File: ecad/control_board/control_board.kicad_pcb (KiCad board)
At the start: 2 copper layers, 40 x 51 mm, 49 parts, among them J1 USB_C_Receptacle_USB2.0_16P, J10 JST PH 3, J2 JST SH 3, J3 JST SH 3, J4 JST SH 3, J5 JST SH 3, J6 JST SH 3, J7 JST SH 3, J9 JST PH 3, Q6 RE1C002UN, U1 W25Q16JVUXIQ, U2 TLV75733PDBV, U3 RP2040, U4 TUSB320I, U5 TPS2552DRV, Y1 ABM8-272-T3

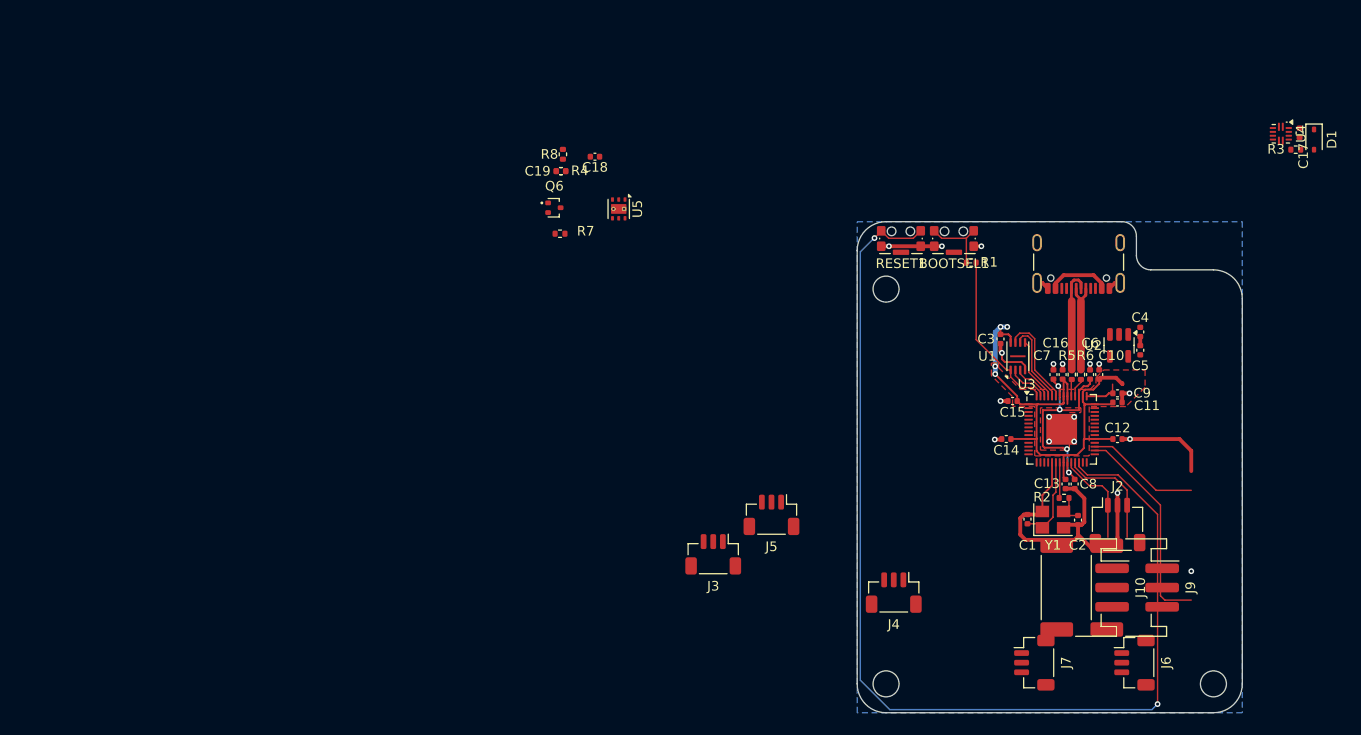
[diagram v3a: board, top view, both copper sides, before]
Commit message: Layouted new control board
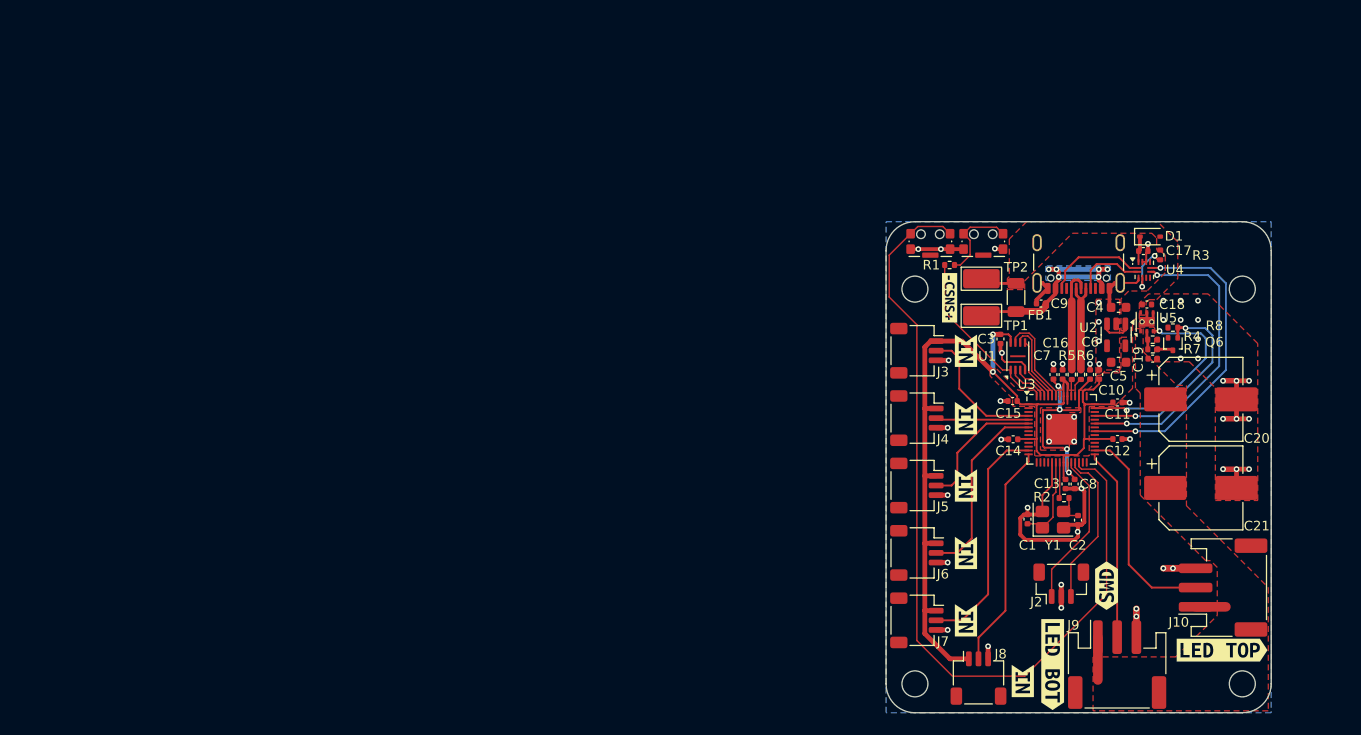
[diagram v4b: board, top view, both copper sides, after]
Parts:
- removed BOOTSEL1, RESET1: CK_KMS2xxG, Button_Switch_SMD:SW_SPST_CK_KMS2xxGP
- added BTN1: CK_KMS2xxG, woodpecker:SW_SPST_CK_KMS2xxGP, F.Cu at (120.1, 52.0)
- added BTN2: CK_KMS2xxG, woodpecker:SW_SPST_CK_KMS2xxGP, F.Cu at (114.6, 52.0)
- added C20: 1u, Capacitor_SMD:CP_Elec_8x10.5, F.Cu at (142.7, 68.5)
- added C21: 1u, Capacitor_SMD:CP_Elec_8x10.5, F.Cu at (142.7, 77.7)
- added FB1: FerriteBead, Resistor_SMD:R_1206_3216Metric, F.Cu at (123.5, 57.9)
- added J8: JST SH 3 Horizontal, woodpecker:JST_SH_SM03B-SRSS-TB_1x03-1MP_P1.00mm_Horizontal, F.Cu at (119.6, 97.4)
- added REF**: MountingHole_2.7mm_M2.5, MountingHole:MountingHole_2.7mm_M2.5, F.Cu at (147.0, 57.0)
- added TP1: 5019, TestPoint:TestPoint_Keystone_5019_Miniature, F.Cu at (119.9, 59.8)
- added TP2: 5019, TestPoint:TestPoint_Keystone_5019_Miniature, F.Cu at (119.9, 55.9)
- added kibuzzard-68C95CAF: G***, kibuzzard-68C95CAF, F.Cu at (132.9, 87.8)
- added kibuzzard-68C95CFD: G***, kibuzzard-68C95CFD, F.Cu at (144.9, 94.5)
- added kibuzzard-68C95D0F: G***, kibuzzard-68C95D0F, F.Cu at (127.3, 96.0)
- added kibuzzard-68C95D22: G***, kibuzzard-68C95D22, F.Cu at (118.3, 91.4)
- added kibuzzard-68C95D22: G***, kibuzzard-68C95D22, F.Cu at (124.2, 97.7)
- added kibuzzard-68C95D22: G***, kibuzzard-68C95D22, F.Cu at (118.3, 84.4)
- added kibuzzard-68C95D22: G***, kibuzzard-68C95D22, F.Cu at (118.3, 63.4)
- added kibuzzard-68C95D22: G***, kibuzzard-68C95D22, F.Cu at (118.3, 77.4)
- added kibuzzard-68C95D22: G***, kibuzzard-68C95D22, F.Cu at (118.3, 70.4)
- added kibuzzard-68C95DDD: G***, kibuzzard-68C95DDD, F.Cu at (116.6, 57.9)
- C4, C5: footprint Capacitor_SMD:C_0402_1005Metric -> Capacitor_SMD:C_0603_1608Metric
- J10, J9: value JST PH 3 -> JST PH 3 Horizontal
- J2: value JST SH 3 -> JST SH 3 Vert; footprint woodpecker:JST_SH_SM03B-SRSS-TB_1x03-1MP_P1.00mm_Horizontal -> woodpecker:JST_SH_BM03B-SRSS-TB_1x03-1MP_P1.00mm_Vertical
- J3, J4, J5, J6, J7: value JST SH 3 -> JST SH 3 Horizontal; footprint woodpecker:JST_SH_BM03B-SRSS-TB_1x03-1MP_P1.00mm_Vertical -> woodpecker:JST_SH_SM03B-SRSS-TB_1x03-1MP_P1.00mm_Horizontal
- moved R8 65.9 mm to (139.8, 61.0), turned to 180 degrees
- moved Q6 65.8 mm to (139.8, 62.7), turned to -90 degrees
- moved C19 64.5 mm to (137.7, 64.2)
- moved R4 63.9 mm to (137.7, 62.2)
- moved R7 62.7 mm to (137.7, 63.2), turned to 0 degrees
- moved C18 59.3 mm to (137.1, 58.6)
- moved U5 56.1 mm to (137.1, 60.4), turned to 90 degrees
- moved J3 29.9 mm to (113.2, 63.4), turned to -90 degrees
- moved J6 25.3 mm to (113.2, 84.4)
- moved C17 20.4 mm to (136.7, 53.0), turned to 0 degrees
- moved U4 20.0 mm to (136.8, 55.0), turned to 0 degrees
- moved D1 19.8 mm to (137.4, 51.5), turned to 0 degrees
- moved J4 18.3 mm to (113.2, 70.4), turned to -90 degrees
- moved R3 17.8 mm to (138.5, 53.5), turned to -90 degrees
- moved J5 15.4 mm to (113.2, 77.4), turned to -90 degrees
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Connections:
- net Net-(Q6-D) renamed /ILIM2_GND
- net Net-(U5-ILIM) renamed /ILIM
- C4 pad 1: +5V -> VBUS
- J10 pad 1: +5V -> +5V_LED
- J10 pad 2: /LED_OUT1 -> /LED_TOP
- J3 pad 2: /RX1 -> /RX0
- J4 pad 2: /RX2 -> /RX1
- J5 pad 2: /RX3 -> /RX2
- J6 pad 2: /RX4 -> /RX3
- J7 pad 2: /RX5 -> /RX4
- J9 pad 1: +5V -> +5V_LED
- J9 pad 2: /LED_OUT0 -> /LED_BOTTOM
- U2 pad 1: +5V -> VBUS
- U2 pad 3: +5V -> VBUS
- U3 pad 13: unconnected-(U3-GPIO10-Pad13) -> /RX4
- U3 pad 14: unconnected-(U3-GPIO11-Pad14) -> /RX5
- U3 pad 29: unconnected-(U3-GPIO18-Pad29) -> /LED_BOTTOM
- U3 pad 30: unconnected-(U3-GPIO19-Pad30) -> /LED_TOP
- U3 pad 35: unconnected-(U3-GPIO23-Pad35) -> /USB_OUT2
- U3 pad 37: unconnected-(U3-GPIO25-Pad37) -> /USB_OUT1
- U3 pad 39: unconnected-(U3-GPIO27_ADC1-Pad39) -> /LED_FULL_EN
- U3 pad 4: unconnected-(U3-GPIO2-Pad4) -> /RX0
- U3 pad 41: unconnected-(U3-GPIO29_ADC3-Pad41) -> /~{LED_FAULT}
- U3 pad 5: unconnected-(U3-GPIO3-Pad5) -> /RX1
- U3 pad 6: unconnected-(U3-GPIO4-Pad6) -> /RX2
- U3 pad 7: unconnected-(U3-GPIO5-Pad7) -> /RX3
- U4 pad 1: /CC1 -> /CC2
- U4 pad 2: /CC2 -> /CC1
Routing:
- net +3V3: track 56.0 -> 98.8 mm, vias 4 -> 2
- net /USB_OUT2: track 0.00 -> 33.7 mm, vias 0 -> 2
- net /USB_OUT1: track 0.00 -> 31.5 mm, vias 0 -> 2
- net (no net): track 25.8 -> 0.00 mm
- net /RUN: track 115.1 -> 89.5 mm, vias 2 -> 0
- net /RX4: track 0.00 -> 24.5 mm
- net GND: track 66.0 -> 90.3 mm, vias 18 -> 53
- net /RX5: track 0.00 -> 23.4 mm
- net /LED_FULL_EN: track 0.00 -> 22.4 mm, vias 0 -> 2
- net /LED_TOP: track 0.00 -> 22.2 mm
- net /~{LED_FAULT}: track 0.00 -> 21.7 mm, vias 0 -> 2
- net /LED_BOTTOM: track 0.00 -> 20.0 mm
- net /RX3: track 0.00 -> 19.7 mm
- net /VBUS_UNFLT: track 6.57 -> 23.9 mm, vias 0 -> 6
- net /RX0: track 0.00 -> 14.2 mm
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- added copper zone on F.Cu, net +5V_LED
- added copper zone on B.Cu, net /VBUS_UNFLT
- added copper zone on F.Cu, net GND
- added copper zone on F.Cu, net VBUS
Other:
- outline, holes or cut-outs redrawn

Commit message: Adds a first logo
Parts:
- added REF**: OSHW-Logo_11.4x12mm_SilkScreen, Symbol:OSHW-Logo_11.4x12mm_SilkScreen, B.Cu at (30.7, 42.8)
- added kibuzzard-68C98DA6: G***, kibuzzard-68C98DA6, B.Cu at (48.1, 65.5)
- C20, C21: value 1u -> 1000u
- C9: footprint Capacitor_SMD:C_0402_1005Metric -> Capacitor_SMD:C_0603_1608Metric
- R3: value 900k -> 910k
- moved R6 92.4 mm to (40.2, 44.9)
- moved U3 92.4 mm to (38.2, 50.6)
- moved BTN1 92.4 mm to (30.1, 31.1)
- moved BTN2 92.4 mm to (24.6, 31.1)
- moved C1 92.4 mm to (34.7, 59.9)
- moved C11 92.4 mm to (44.0, 47.8)
- moved C12 92.4 mm to (44.0, 51.6)
- moved C14 92.4 mm to (33.2, 51.6)
- moved C15 92.4 mm to (33.1, 47.6)
- moved C16 92.4 mm to (38.3, 44.9)
- moved C17 92.4 mm to (46.7, 32.0)
- moved C18 92.4 mm to (47.1, 37.6)
- moved C19 92.4 mm to (47.7, 43.2)
- moved C2 92.4 mm to (39.9, 60.0)
- moved C3 92.4 mm to (31.9, 41.2)
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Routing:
- net /VBUS_UNFLT: track 23.9 -> 25.0 mm
- added copper zone on F.Cu, net /VBUS_UNFLT
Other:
- board text added: "0"
- board text added: "0 mm"
- board text added: "0.01 mm"
- board text added: "0.02"
- board text added: "0.035 mm"
- board text added: "0.1500 mm / 0.1500 mm"
- board text added: "0.3000 mm"
- board text added: "0.91 mm"
- board text added: "1"
- board text added: "1.0000 mm"
- board text added: "2"
- board text added: "3.3"
- board text added: "4.5"
- board text added: "40.0000 mm x 51.0000 mm"
- board text added: "B.Cu"
- board text added: "B.Mask"
- board text added: "B.Paste"
- board text added: "B.Silkscreen"
- board text added: "BOARD CHARACTERISTICS"
- board text added: "Board Thickness:"
- board text added: "Board overall dimensions:"
- board text added: "Bottom Silk Screen"
- board text added: "Bottom Solder Mask"
- board text added: "Bottom Solder Paste"
- board text added: "Castellated pads:"
- board text added: "Color"
- board text added: "Copper Finish:"
- board text added: "Copper Layer Count:"
- board text added: "Dielectric"
- board text added: "Edge card connectors:"
- board text added: "Epsilon R"
- board text added: "F.Cu"
- board text added: "F.Mask"
- board text added: "F.Paste"
- board text added: "F.Silkscreen"
- board text added: "FR4"
- board text added: "Green"
- board text added: "Impedance Control:"
- board text added: "Layer Name"
- board text added: "Loss Tangent"
- board text added: "Material"
- board text added: "Min hole diameter:"
- board text added: "Min track/spacing:"
- board text added: "No"
- board text added: "None"
- board text added: "Not specified"
- board text added: "Plated Board Edge:"
- board text added: "Thickness (mm)"
- board text added: "Top Silk Screen"
- board text added: "Top Solder Mask"
- board text added: "Top Solder Paste"
- board text added: "Type"
- board text added: "USB C 2.0"
- board text added: "WayWayWay"
- board text added: "Yes"
- board text added: "copper"
- board text added: "core"
- board text added: "© 2025 Alexandre Tuleu"

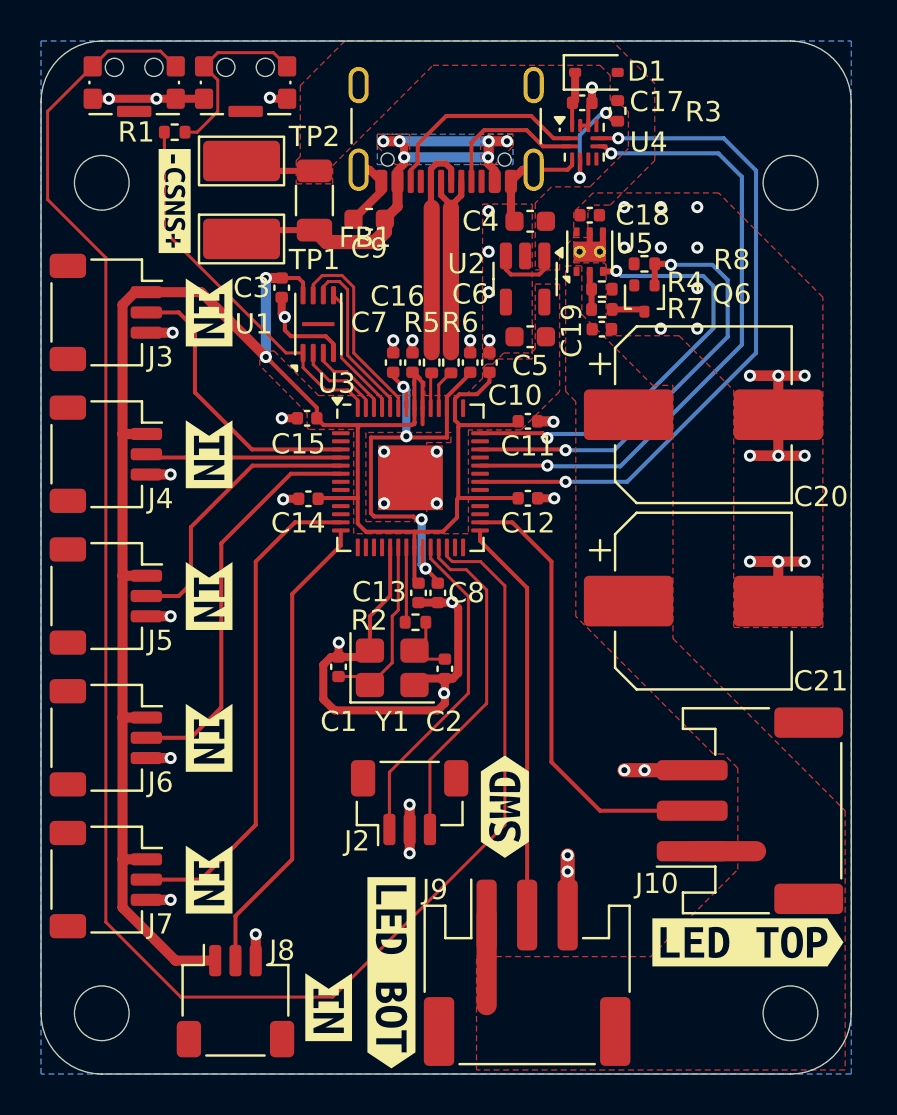
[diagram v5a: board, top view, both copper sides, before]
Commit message: Updated Controller for I2C controlled LED Matrices
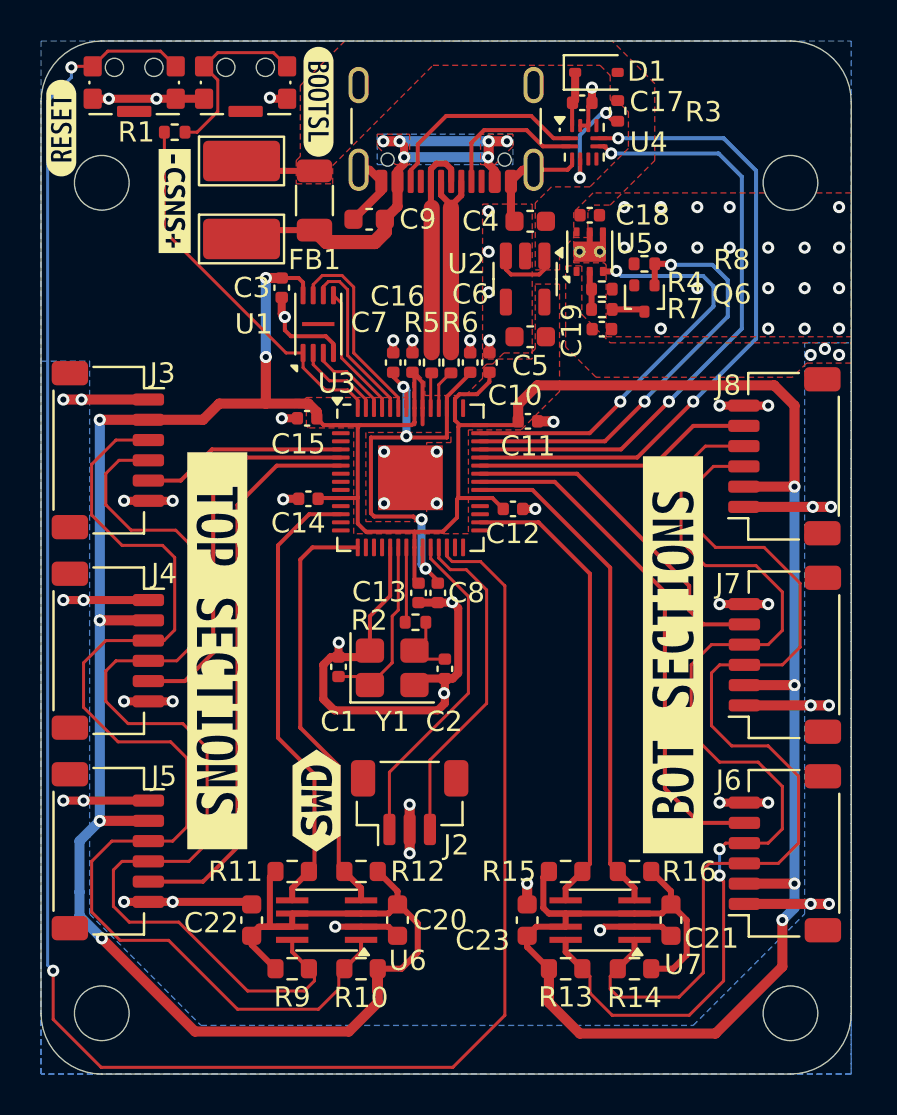
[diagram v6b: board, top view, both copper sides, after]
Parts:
- removed J10, J9: JST PH 3 Horizontal, woodpecker:JST_PH_S3B-PH-SM4-TB_1x03-1MP_P2.00mm_Horizontal
- removed kibuzzard-68C95CFD: G***, kibuzzard-68C95CFD
- removed kibuzzard-68C95D0F: G***, kibuzzard-68C95D0F
- removed kibuzzard-68C95D22 (x6): G***, kibuzzard-68C95D22
- added C22: 100n, Capacitor_SMD:C_0603_1608Metric, F.Cu at (30.4, 72.4)
- added C23: 100n, Capacitor_SMD:C_0603_1608Metric, F.Cu at (44.0, 72.4)
- added R10: 2.2k, Resistor_SMD:R_0603_1608Metric, F.Cu at (35.8, 74.8)
- added R11: 3.3k, Resistor_SMD:R_0603_1608Metric, F.Cu at (32.4, 70.0)
- added R12: 3.3k, Resistor_SMD:R_0603_1608Metric, F.Cu at (35.8, 70.0)
- added R13: 2.2k, Resistor_SMD:R_0603_1608Metric, F.Cu at (45.9, 74.8)
- added R14: 2.2k, Resistor_SMD:R_0603_1608Metric, F.Cu at (49.3, 74.8)
- added R15: 3.3k, Resistor_SMD:R_0603_1608Metric, F.Cu at (45.9, 70.0)
- added R16: 3.3k, Resistor_SMD:R_0603_1608Metric, F.Cu at (49.3, 70.0)
- added R9: 2.2k, Resistor_SMD:R_0603_1608Metric, F.Cu at (32.4, 74.8)
- added U6: TCA9406DCTR, Package_SO:SSOP-8_2.95x2.8mm_P0.65mm, F.Cu at (34.1, 72.4)
- added U7: TCA9406DCTR, Package_SO:SSOP-8_2.95x2.8mm_P0.65mm, F.Cu at (47.6, 72.4)
- added kibuzzard-68CC7F6C: G***, kibuzzard-68CC7F6C, F.Cu at (51.2, 59.3)
- added kibuzzard-68CC7F87: G***, kibuzzard-68CC7F87, F.Cu at (28.7, 59.1)
- added kibuzzard-68CC835E: G***, kibuzzard-68CC835E, F.Cu at (21.0, 33.3)
- added kibuzzard-68CC8382: G***, kibuzzard-68CC8382, F.Cu at (33.7, 32.0)
- C20, C21: value 1000u -> 100n; footprint Capacitor_SMD:CP_Elec_8x10.5 -> Capacitor_SMD:C_0603_1608Metric
- J3, J4, J5, J6, J7, J8: value JST SH 3 Horizontal -> JST SH 6P; footprint woodpecker:JST_SH_SM03B-SRSS-TB_1x03-1MP_P1.00mm_Horizontal -> Connector_JST:JST_SH_SM06B-SRSS-TB_1x06-1MP_P1.00mm_Horizontal
- moved J8 38.2 mm to (56.7, 49.5), turned to 90 degrees
- moved J7 35.3 mm to (56.7, 59.3), turned to 90 degrees
- moved J6 34.0 mm to (56.7, 69.1), turned to 90 degrees
- moved C20 29.2 mm to (37.6, 72.4), turned to -90 degrees
- moved C21 15.8 mm to (51.1, 72.4), turned to -90 degrees
- moved J5 12.6 mm to (23.3, 69.0)
- moved J4 9.70 mm to (23.3, 59.1)
- moved kibuzzard-68C95CAF 9.30 mm to (33.6, 66.5)
- moved J3 6.80 mm to (23.3, 49.2)
- moved C12 0.91 mm to (43.3, 52.1)
- moved REF** 0.90 mm to (30.7, 43.7)
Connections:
- C20 pad 1: +5V_LED -> +3V3
- C21 pad 1: +5V_LED -> +3V3
- J3 pad 1: +3V3 -> +5V_LED
- J3 pad 2: /RX0 -> +3V3
- J3 pad 3: GND -> /SDA0
- J4 pad 1: +3V3 -> +5V_LED
- J4 pad 2: /RX1 -> +3V3
- J4 pad 3: GND -> /SDA0
- J5 pad 1: +3V3 -> +5V_LED
- J5 pad 2: /RX2 -> +3V3
- J5 pad 3: GND -> /SDA0
- J6 pad 1: +3V3 -> +5V_LED
- J6 pad 2: /RX3 -> +3V3
- J6 pad 3: GND -> /SDA1
- J7 pad 1: +3V3 -> +5V_LED
- J7 pad 2: /RX4 -> +3V3
- J7 pad 3: GND -> /SDA1
- J8 pad 1: +3V3 -> +5V_LED
- J8 pad 2: /RX5 -> +3V3
- J8 pad 3: GND -> /SDA1
- U3 pad 12: unconnected-(U3-GPIO9-Pad12) -> /RP_SCL0
- U3 pad 13: /RX4 -> unconnected-(U3-GPIO10-Pad13)
- U3 pad 14: /RX5 -> unconnected-(U3-GPIO11-Pad14)
- U3 pad 15: unconnected-(U3-GPIO12-Pad15) -> /RP_SDA0
- U3 pad 29: /LED_BOTTOM -> unconnected-(U3-GPIO18-Pad29)
- U3 pad 30: /LED_TOP -> /RP_SCL1
- U3 pad 34: unconnected-(U3-GPIO22-Pad34) -> /RP_SDA1
- U3 pad 35: /USB_OUT2 -> /RX3
- U3 pad 36: unconnected-(U3-GPIO24-Pad36) -> /RX4
- U3 pad 37: /USB_OUT1 -> /RX5
- U3 pad 38: unconnected-(U3-GPIO26_ADC0-Pad38) -> /USB_OUT2
- U3 pad 39: /LED_FULL_EN -> /USB_OUT1
- U3 pad 40: unconnected-(U3-GPIO28_ADC2-Pad40) -> /LED_FULL_EN
- U3 pad 7: /RX3 -> unconnected-(U3-GPIO5-Pad7)
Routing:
- net +3V3: track 98.8 -> 218.3 mm, vias 2 -> 10
- net /SDA0: track 0.00 -> 56.6 mm
- net /SCL1: track 0.00 -> 52.3 mm, vias 0 -> 2
- net /SCL0: track 0.00 -> 52.1 mm
- net /SDA1: track 0.00 -> 48.8 mm
- net /RP_SDA1: track 0.00 -> 24.9 mm
- net /RP_SCL1: track 0.00 -> 23.1 mm
- net /RP_SCL0: track 0.00 -> 22.5 mm
- net /LED_TOP: track 22.2 -> 0.00 mm
- net /RP_SDA0: track 0.00 -> 21.2 mm
- net /LED_BOTTOM: track 20.0 -> 0.00 mm
- net +5V_LED: track 7.60 -> 25.2 mm, vias 0 -> 15
- net /RX2: track 13.9 -> 27.9 mm
- net /RUN: track 89.5 -> 102.8 mm, vias 0 -> 2
- net /RX5: track 23.4 -> 13.8 mm
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- added copper zone on B.Cu, net +5V_LED

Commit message: First production run for PCB
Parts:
- added J9: JST SH, woodpecker:JST_SH_SM03B-SRSS-TB_1x03-1MP_P1.00mm_Horizontal, B.Cu at (23.4, 43.1)
- added kibuzzard-68CD18AE: G***, kibuzzard-68CD18AE, B.Cu at (27.7, 43.1)
- J2: footprint woodpecker:JST_SH_BM03B-SRSS-TB_1x03-1MP_P1.00mm_Vertical -> woodpecker:JST_SH_SM03B-SRSS-TB_1x03-1MP_P1.00mm_Horizontal
- J3, J4, J5, J6, J7, J8: footprint Connector_JST:JST_SH_SM06B-SRSS-TB_1x06-1MP_P1.00mm_Horizontal -> woodpecker:JST_SH_SM06B-SRSS-TB_1x06-1MP_P1.00mm_Horizontal
- kibuzzard-68CC835E, kibuzzard-68CC8382: moved to B.Cu
- moved kibuzzard-68C98DA6 7.15 mm to (52.9, 60.1)
- moved REF** 5.35 mm to (36.0, 43.4)
- moved kibuzzard-68CC8382 3.74 mm to (30.1, 33.0), turned to 0 degrees
- moved kibuzzard-68CC835E 3.61 mm to (24.6, 33.0), turned to 0 degrees
- moved J2 2.72 mm to (40.9, 66.3)
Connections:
- U3 pad 2: unconnected-(U3-GPIO0-Pad2) -> /UART_TX
- U3 pad 3: unconnected-(U3-GPIO1-Pad3) -> /UART_RX
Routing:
- net /UART_TX: track 0.00 -> 13.0 mm, vias 0 -> 1
- net /UART_RX: track 0.00 -> 11.7 mm, vias 0 -> 1
- net +3V3: track 218.3 -> 225.9 mm, vias 10 -> 11
- net /SWDIO: track 16.5 -> 11.7 mm
- net /SWCLK: track 16.3 -> 11.6 mm
